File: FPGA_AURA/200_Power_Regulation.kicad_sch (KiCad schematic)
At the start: 45 parts, among them U4 ADP5014, U6 NCP51200MNTXG

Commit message: Initial component selection done
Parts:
- removed C15, C16, C17: 47u, Capacitor_SMD:C_0402_1005Metric, symbol Device:C
- removed L1: 1u, Inductor_SMD:L_Changjiang_FXL0420, symbol Device:L
- removed R24: 121k, Resistor_SMD:R_0402_1005Metric, symbol Device:R
- added C200, C201, C202, C203: 10u, Capacitor_SMD:C_0603_1608Metric, symbol Device:C
- added C207, C208, C209: 47u, Capacitor_SMD:C_0805_2012Metric, symbol Device:C
- added C220: 1u, Capacitor_SMD:C_0402_1005Metric, symbol Device:C
- added L201: 1u, Inductor_SMD:L_Chilisin_BMRB00050518-B, symbol Device:L
- added R203: 56k2, Resistor_SMD:R_0402_1005Metric, symbol Device:R
- C206: renamed from C14; footprint Capacitor_SMD:C_0402_1005Metric -> Capacitor_SMD:C_0805_2012Metric
- L200: renamed from L4; footprint Inductor_SMD:L_1210_3225Metric -> Inductor_SMD:L_Chilisin_BMRB00050518-B
- R202: renamed from R23; value 121k -> 0R
- R219: renamed from R29; value 4k9 -> 47k
- renumbered C7 to C205, C21 to C210, C20 to C211, C19 to C212, C18 to C213, C10 to C214, C13 to C215, C11 to C216, C12 to C217, C8 to C218, C9 to C219, L2 to L202, L3 to L203, R21 to R200, R22 to R201, R17 to R204, R16 to R205, R18 to R206, R8 to R207, R7 to R208, R12 to R209, R13 to R210, R14 to R211, R15 to R212, R19 to R213, R20 to R214, R28 to R215, R27 to R216, R26 to R217, R25 to R218, R11 to R220, R9 to R221, R6 to R222, R10 to R223, U4 to U200, U6 to U201
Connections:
- net +1V35: now also C208.1
- net +1V8: now also C207.1, L201.2
- net +3V3: now also C209.1
- net +5V_FILT: now also C200.1, C201.1, C202.1, C203.1, C220.1
- net ADP_SW2: now also L201.1
- net GND: now also C200.2, C201.2, C202.2, C203.2, C207.2, C208.2, C209.2, C220.2, R203.1
- net ADP_EN4: now reaches U200.12 (EN4/DL34)
- net ADP_EN4: now also R203.2
- net ADP_EN2: now reaches R202.2, U200.16 (EN2/DL12)
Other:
- note added: "All resistors must be 1% FB = VSETx = Vref(R2/(R1+R2)), where Vref=2V0 For 3V3, tie Vset to 2V0 and use PD on FB L = (Vin - Vout)(Vout/Vin)/(0.3I * fsw) Compensation network assumes maximum current draw on each channel due to the unpredictable FPGA current draw Power Sequence 1V0 @ 0ms, 1V8 @ 6ms, 1V35 @ 12ms, 3V3 @ 12ms"
- note added: "RT: 1MHz CFG1: 4A, 4A, 2A, 2A CFG2: Sequnce, 1x, FPWM, UVO EN3/UV: 3V9 cut-off EN2/DL12: 2ms (soft start), 6ms EN4/DL34: 12ms, 12ms"
- note added: "ToDo: Validate component values Validate power up sequence"
- note removed: "Power Sequence 1V0 18ms -> 1V8 18ms -> 1V35 18ms -> 3V3 Compensation network assumes maximum current draw on each channel due to the unpredictable FPGA current draw Vout = Vref(R2/(R1+R2)), where Vref=2V0 L = (Vin - Vout)(Vout/Vin)/(0.3I * fsw) For 3V3, tie Vset to 2V0 and use PD on FB"
- note removed: "Validate Component values Fix power sequencing (it is not correct)"
- moved on the sheet: C205, C206, C210, C211, C212, C213, C214, C215, C216, C217, C218, C219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

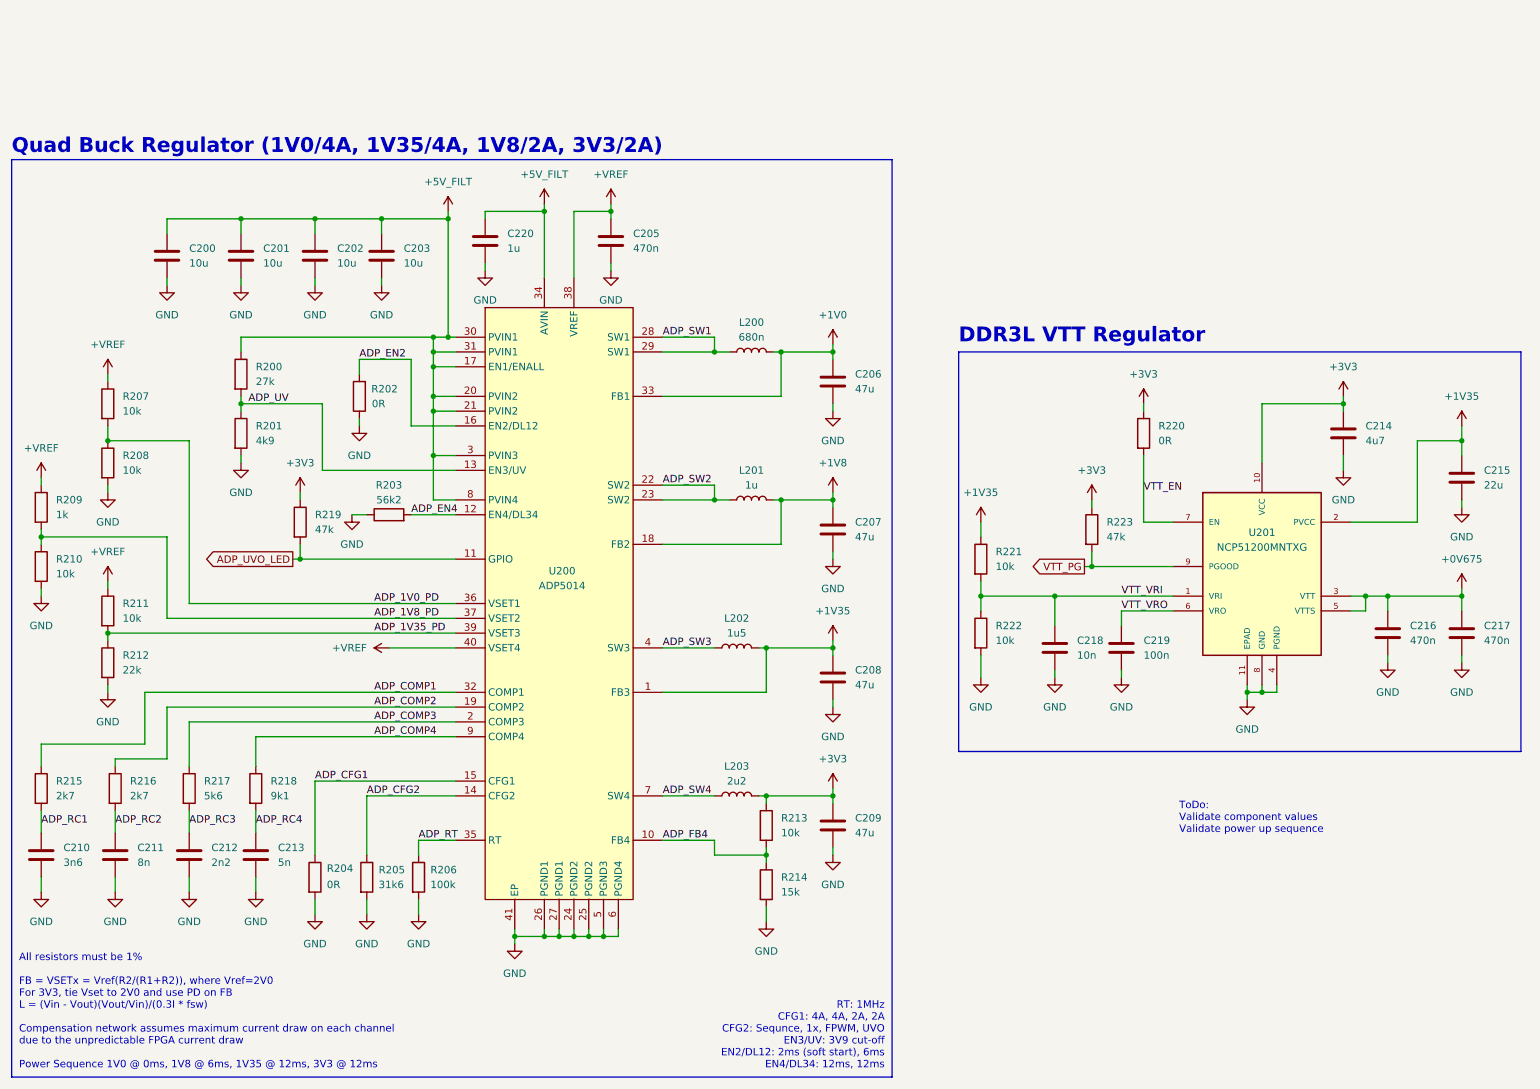
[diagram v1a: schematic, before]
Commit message: Added USB power schottky and started DDR3L
Transferring from laptop to PC to decide DDR3 pins.
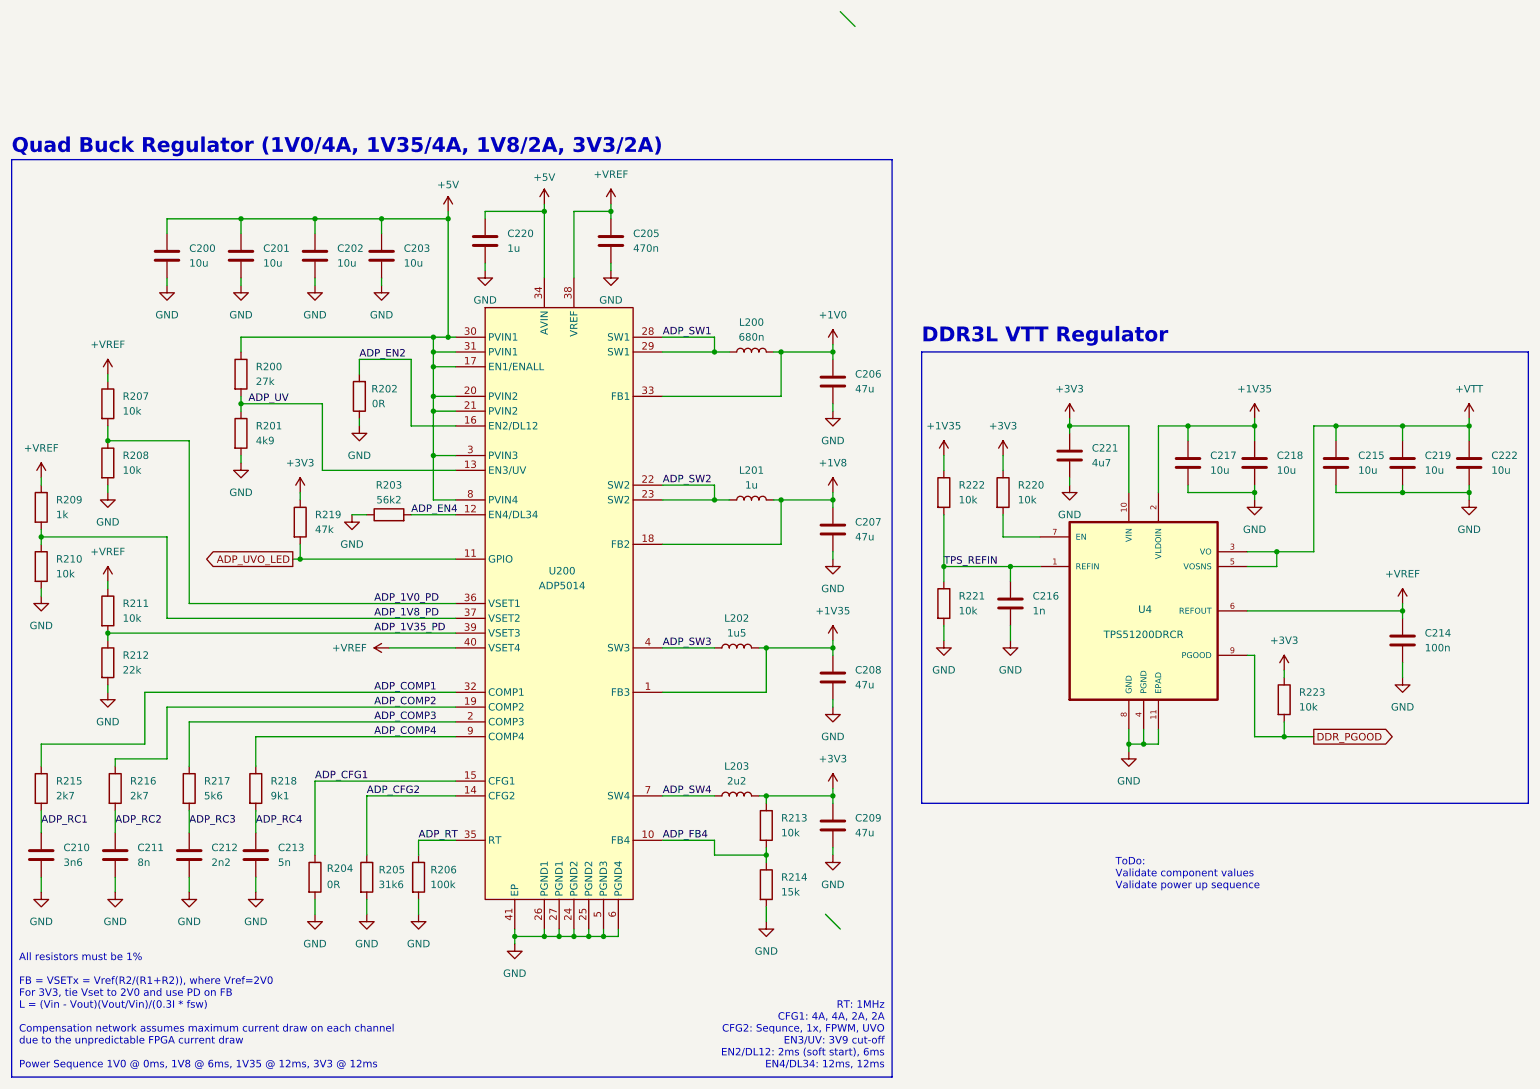
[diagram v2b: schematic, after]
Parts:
- removed U201: NCP51200MNTXG, NCP51200MNTXG:SON50P300X300X100-11N, symbol NCP51200MNTXG:NCP51200MNTXG
- added C221: 4u7, Capacitor_SMD:C_0402_1005Metric, symbol Device:C
- added C222: 10u, Capacitor_SMD:C_0402_1005Metric, symbol Device:C
- added U4: TPS51200DRCR, TPS51200DRCR:VREG_V62_16624-01YE, symbol TPS51200DRCR:TPS51200DRCR
- C214: value 4u7 -> 100n
- C215: value 22u -> 10u
- C216: value 470n -> 1n
- C217: value 470n -> 10u
- C218: value 10n -> 10u
- C219: value 100n -> 10u
- R220: value 0R -> 10k
- R223: value 47k -> 10k
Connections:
- net +1V35: now also C217.1, C218.1, R222.1, U4.2 (VLDOIN); no longer C215.1, R221.1
- net +3V3: now also C221.1, U4.10 (VIN); no longer C214.1
- net +VREF: now also C214.1, U4.6 (REFOUT)
- net GND: now also R221.2, C221.2, C222.2, U4.11 (EPAD), U4.4 (PGND), U4.8 (GND); no longer R222.2
- net +0V675 renamed TPS_REFIN
- net TPS_REFIN: now also R221.1, R222.2, U4.1 (REFIN); no longer C217.1
- net +5V_FILT renamed +5V
- net VTT_EN: no longer names the net of R220.2
- net VTT_EN: now also U4.7 (EN)
- net VTT_PG renamed DDR_PGOOD
- net DDR_PGOOD: now also U4.9 (PGOOD)
- removed net VTT_VRI: C218.1, R221.2, R222.1
- net VTT_VRO renamed +VTT
- net +VTT: now also C215.1, C222.1, U4.3 (VO), U4.5 (VOSNS)
